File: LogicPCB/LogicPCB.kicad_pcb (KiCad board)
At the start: 4 copper layers, 53.6 x 60 mm, 71 parts, among them IC1 DRV8411PWPR, IC2 DRV8411PWPR, IC3 DRV8411PWPR, J1 POWER_IN, J3 DC_OUT, J4 ICSP, J5 RS232, SW1 SW_Push_Dual, U1 DRV8871DDA, U2 ATmega2560-16A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

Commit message: LogicPCB done
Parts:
- removed D1: 1N5819, Diode_THT:D_DO-41_SOD81_P10.16mm_Horizontal
- removed TP3: TestPoint, TestPoint:TestPoint_Pad_D1.0mm
- moved U5 111.1 mm to (94.8, 137.1)
- moved SW1 111.0 mm to (94.8, 156.9), turned to -90 degrees
- moved U3 107.8 mm to (94.2, 130.6), turned to 180 degrees
- moved R13 97.9 mm to (93.7, 148.9), turned to 180 degrees
- moved J4 97.2 mm to (115.0, 145.8)
- moved C24 96.6 mm to (90.6, 136.9), turned to -90 degrees
- moved R17 94.1 mm to (96.9, 116.3)
- moved R18 94.1 mm to (96.9, 120.1)
- moved R19 94.1 mm to (96.9, 123.9)
- moved R14 89.7 mm to (96.9, 118.2)
- moved R15 89.7 mm to (96.9, 122.0)
- moved R16 89.7 mm to (96.9, 125.8)
- moved C13 89.4 mm to (93.0, 150.4), turned to 180 degrees
- moved U4 87.8 mm to (106.2, 148.2), turned to 90 degrees
- moved C17 83.8 mm to (103.0, 153.5), turned to 180 degrees
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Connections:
- IC3 pad 8: /FAULT_STP23 -> /FAULT_STP3
- J1 pad 2: Net-(D1-A) -> VM
- J3 pad 1: OUT1_DC -> OUT2_DC
- J3 pad 2: OUT2_DC -> OUT1_DC
- R10 pad 1: /FAULT_STP23 -> /FAULT_STP3
- U2 pad 53: /FAULT_STP1 -> /SLEEP_STP1
- U2 pad 54: /FAULT_STP2 -> /FAULT_STP1
- U2 pad 55: /FAULT_STP3 -> /SLEEP_STP2
- U2 pad 56: /SLEEP_STP1 -> /FAULT_STP2
- U2 pad 57: /SLEEP_STP2 -> /SLEEP_STP3
- U2 pad 58: /SLEEP_STP3 -> /FAULT_STP3
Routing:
- net +5V: track 0.00 -> 176.5 mm, vias 0 -> 2
- net /SLEEP_STP1: track 0.00 -> 77.5 mm, vias 0 -> 3
- net /SLEEP_STP3: track 0.00 -> 63.2 mm, vias 0 -> 3
- net /FAULT_STP1: track 0.00 -> 61.9 mm, vias 0 -> 2
- net /RESET: track 0.00 -> 59.1 mm, vias 0 -> 1
- net /SLEEP_STP2: track 0.00 -> 59.0 mm, vias 0 -> 3
- net /FAULT_STP3: track 0.00 -> 54.6 mm, vias 0 -> 2
- net /FAULT_STP2: track 0.00 -> 51.9 mm, vias 0 -> 2
- net /BIN1_STP1: track 0.00 -> 50.9 mm, vias 0 -> 2
- net /AIN1_STP3: track 0.00 -> 48.1 mm, vias 0 -> 2
- net GND: track 8.98 -> 55.9 mm, vias 111 -> 128
- net /BIN1_STP3: track 0.00 -> 46.3 mm, vias 0 -> 2
- net /AIN2_STP1: track 0.00 -> 45.4 mm, vias 0 -> 2
- net /AIN1_STP1: track 0.00 -> 45.0 mm, vias 0 -> 2
- net /BIN2_STP1: track 0.00 -> 44.8 mm, vias 0 -> 2
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- added copper zone on F.Cu, net +5V
- removed copper zone on B.Cu, net OUT1_DC
- removed copper zone on B.Cu, net OUT2_DC
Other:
- board size 53.6 x 60 mm -> 65.6 x 64.6 mm
- copper layers 4 -> 2
- board text added: "POWER ON"
- board text added: "SLEEP FAULT"
- board text added: "STP1"
- board text added: "STP2"
- board text added: "STP3"
- board text removed: "DC_OUT"

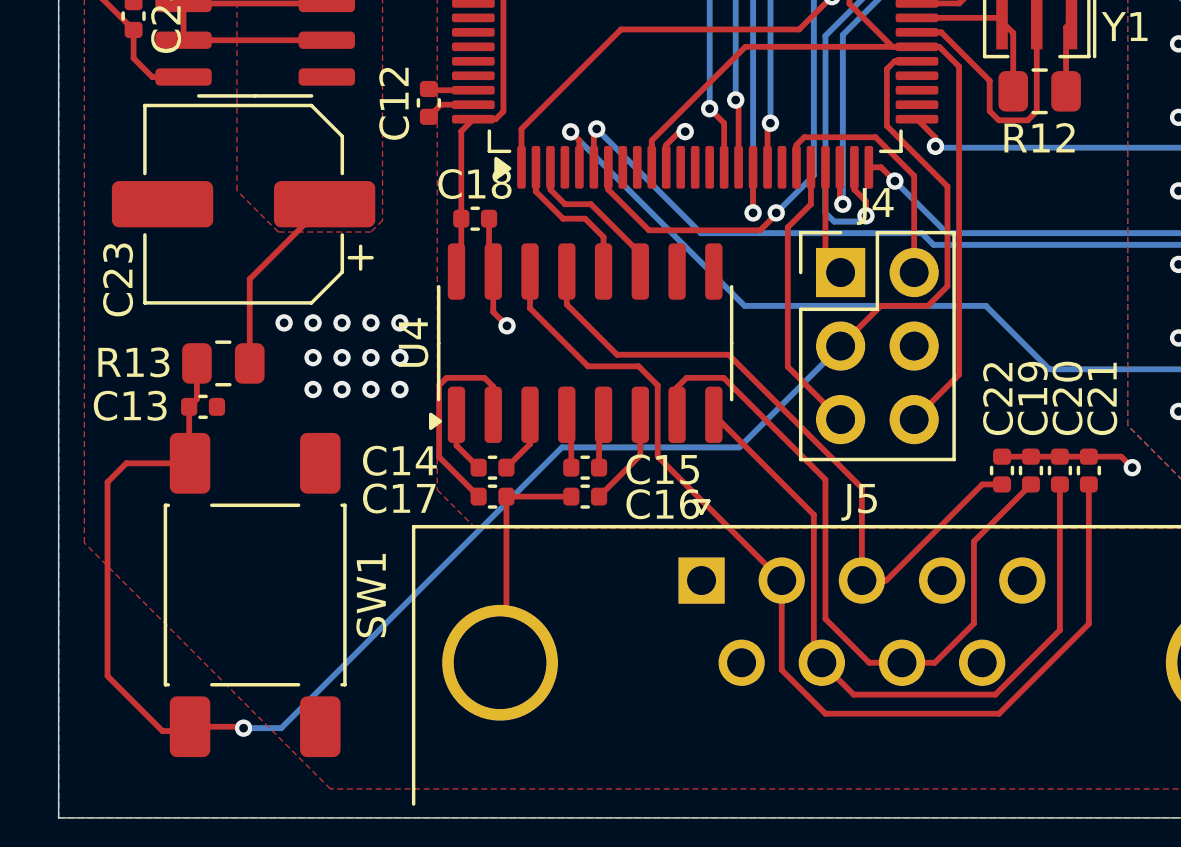
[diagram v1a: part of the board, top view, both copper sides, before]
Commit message: Minor silkscreen fixes
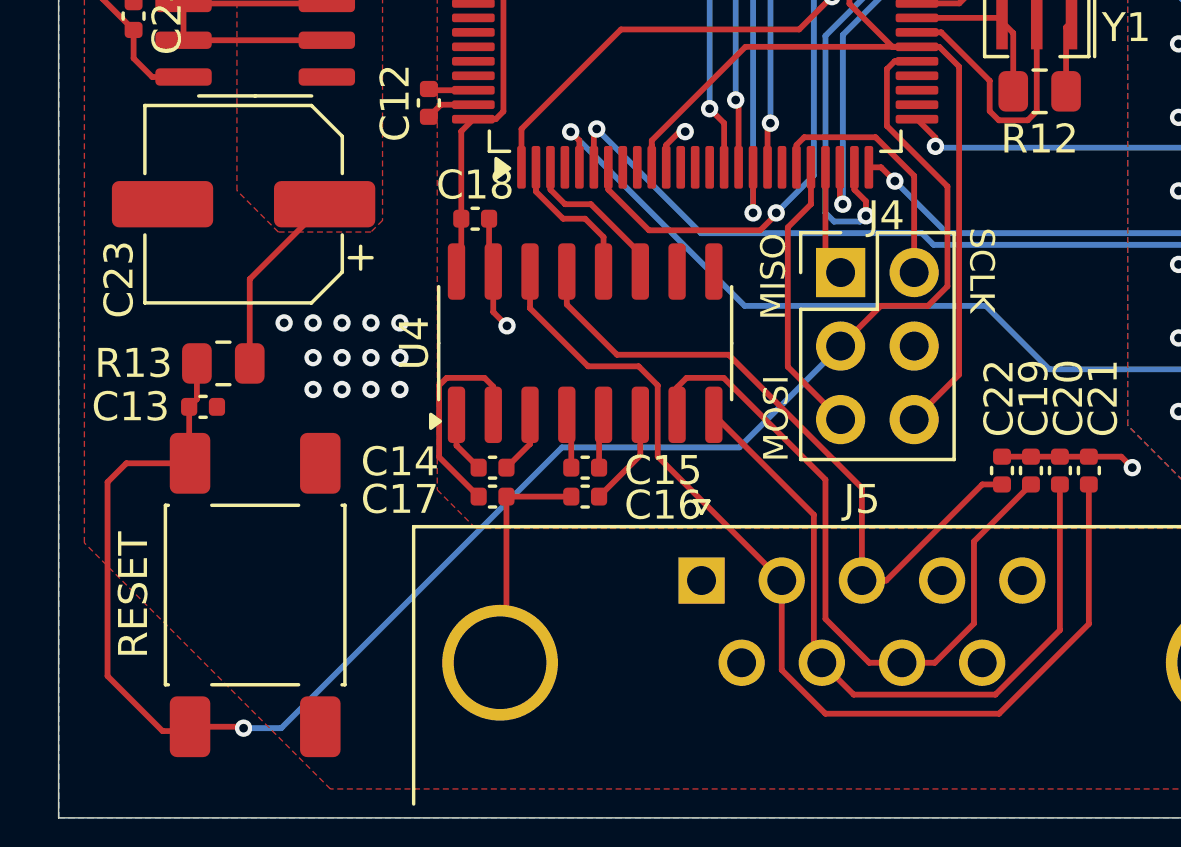
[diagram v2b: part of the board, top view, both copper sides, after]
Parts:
- renumbered SW1 to RESET
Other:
- board text added: "MISO"
- board text added: "MOSI"
- board text added: "SCLK"
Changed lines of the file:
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@@
 		(tags "Through hole pin header THT 2x03 2.54mm double row")
 		(property "Reference" "J4"
-			(at 1.27 -2.38 0)
+			(at 1.575 -1.96 0)
 			(layer "F.SilkS")
 			(effects
@@
 		(descr "Tactile switch, 6x6 mm, H4.3 mm, gullwing terminals, https://www.e-switch.com/wp-content/uploads/2024/03/TL3301.pdf")
 		(tags "SPST button straight")
-		(property "Reference" "SW1"
-			(at 0 -4.05 90)
+		(property "Reference" "RESET"
+			(at 0 4.2 270)
 			(layer "F.SilkS")
 			(effects
@@
 		(layer "Edge.Cuts")
 	)
+	(gr_text "SCLK"
+		(at 119.4 144.2 270)
+		(layer "F.SilkS")
+		(effects
+			(font
+				(size 0.85 0.85)
+				(thickness 0.1)
+			)
+			(justify left bottom)
+		)
+	)
 	(gr_text "SLEEP\nFAULT"
 		(at 103.2 122.535 0)
@@
 		)
 	)
+	(gr_text "MOSI"
+		(at 113.3 152.3 90)
+		(layer "F.SilkS")
+		(effects
+			(font
+				(size 0.85 0.85)
+				(thickness 0.1)
+			)
+			(justify left bottom)
+		)
+	)
 	(gr_text "POWER ON"
 		(at 143.1 105.4 0)
@@
 				(thickness 0.1)
 			)
+			(justify left bottom)
+		)
+	)
+	(gr_text "MISO"
+		(at 113.2 147.4 90)
+		(layer "F.SilkS")
+		(effects
+			(font
+				(size 0.85 0.85)
+				(thickness 0.1)
+			)

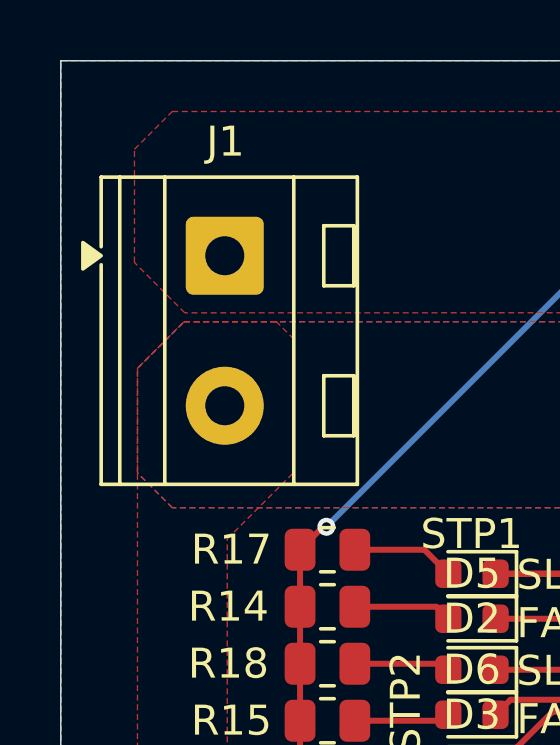
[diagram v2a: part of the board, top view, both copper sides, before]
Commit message: Add power polarity indicators
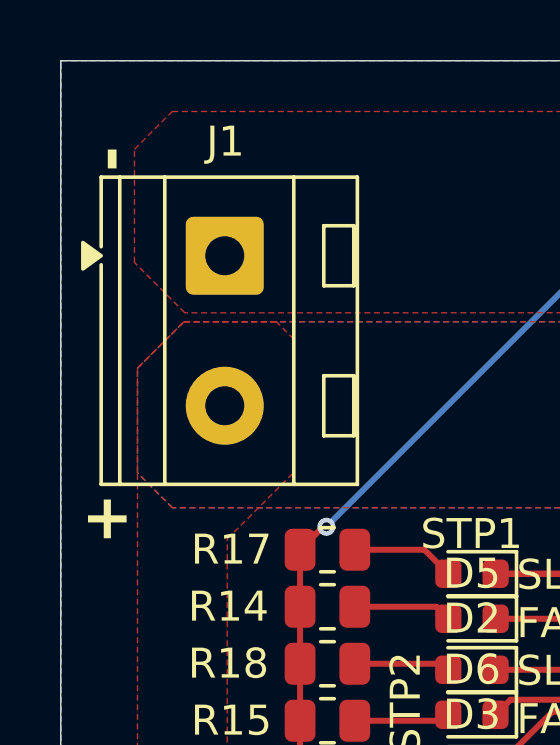
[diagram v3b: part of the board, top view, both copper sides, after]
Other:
- board text added: "+"
- board text added: "-"
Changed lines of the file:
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@@
+		)
+	)
+	(gr_text "+"
+		(at 88.7 116.1 0)
+		(layer "F.SilkS")
+		(effects
+			(font
+				(size 1.5 1.5)
+				(thickness 0.3)
+				(bold yes)
+			)
+			(justify left bottom)
 		)
 	)
@@
 			)
 			(justify left bottom)
+		)
+	)
+	(gr_text "-"
+		(at 90.5 103.7 90)
+		(layer "F.SilkS")
+		(effects
+			(font
+				(size 1.5 1.5)
+				(thickness 0.3)
+				(bold yes)
+			)
+			(justify left bottom)

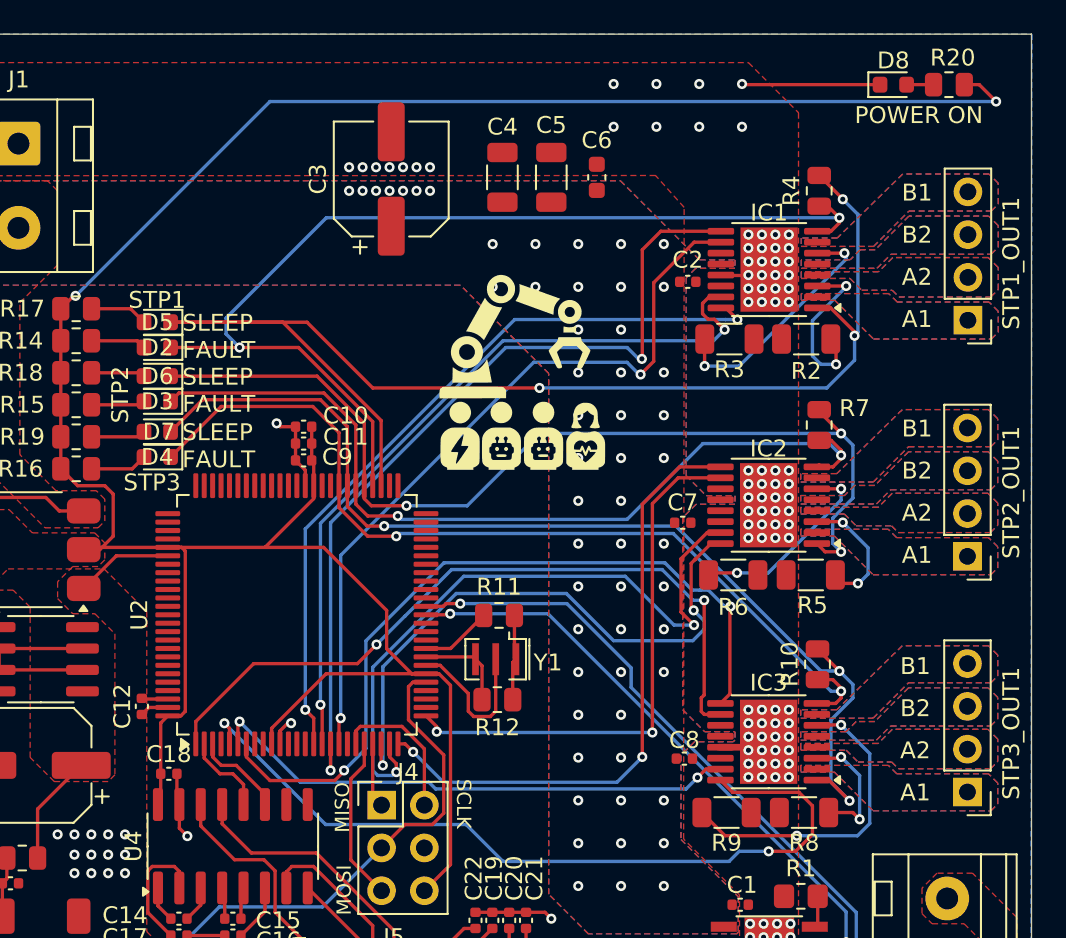
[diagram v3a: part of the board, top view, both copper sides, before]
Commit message: Correct JST header footprint and minor silkscreen changes
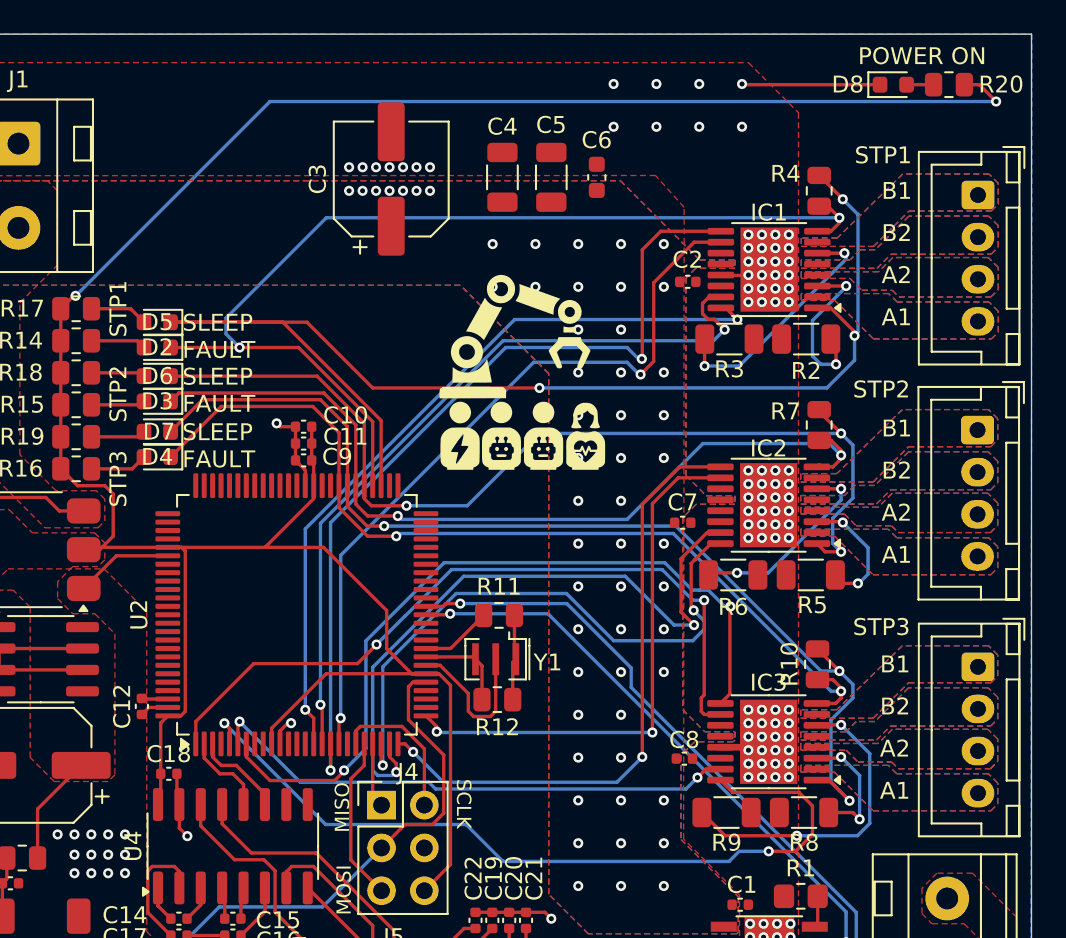
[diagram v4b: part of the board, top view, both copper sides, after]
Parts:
- STP1: renamed from STP1_OUT1; footprint Connector_PinHeader_2.54mm:PinHeader_1x04_P2.54mm_Vertical -> Connector_JST:JST_XH_B4B-XH-A_1x04_P2.50mm_Vertical
- STP2: renamed from STP2_OUT1; footprint Connector_PinHeader_2.54mm:PinHeader_1x04_P2.54mm_Vertical -> Connector_JST:JST_XH_B4B-XH-A_1x04_P2.50mm_Vertical
- STP3: renamed from STP3_OUT1; footprint Connector_PinHeader_2.54mm:PinHeader_1x04_P2.54mm_Vertical -> Connector_JST:JST_XH_B4B-XH-A_1x04_P2.50mm_Vertical
- moved STP2 7.52 mm to (150.4, 123.5), turned to -90 degrees
- moved STP3 7.46 mm to (150.4, 137.6), turned to -90 degrees
- moved STP1 7.45 mm to (150.4, 109.5), turned to -90 degrees
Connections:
- STP1 pad 1: AOUT1_STP1 -> BOUT1_STP1
- STP1 pad 2: AOUT2_STP1 -> BOUT2_STP1
- STP1 pad 3: BOUT2_STP1 -> AOUT2_STP1
- STP1 pad 4: BOUT1_STP1 -> AOUT1_STP1
- STP2 pad 1: AOUT1_STP2 -> BOUT1_STP2
- STP2 pad 2: AOUT2_STP2 -> BOUT2_STP2
- STP2 pad 3: BOUT2_STP2 -> AOUT2_STP2
- STP2 pad 4: BOUT1_STP2 -> AOUT1_STP2
- STP3 pad 1: AOUT1_STP3 -> BOUT1_STP3
- STP3 pad 2: AOUT2_STP3 -> BOUT2_STP3
- STP3 pad 3: BOUT2_STP3 -> AOUT2_STP3
- STP3 pad 4: BOUT1_STP3 -> AOUT1_STP3
